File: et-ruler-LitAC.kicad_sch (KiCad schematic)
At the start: 27 parts, among them J1 Conn_01x03, J2 AudioJack2, J3 Pmod-Interface-GPIO6, J4 Pmod-Interface-GPIO6, SW1 SW_DPDT, U1 OP07

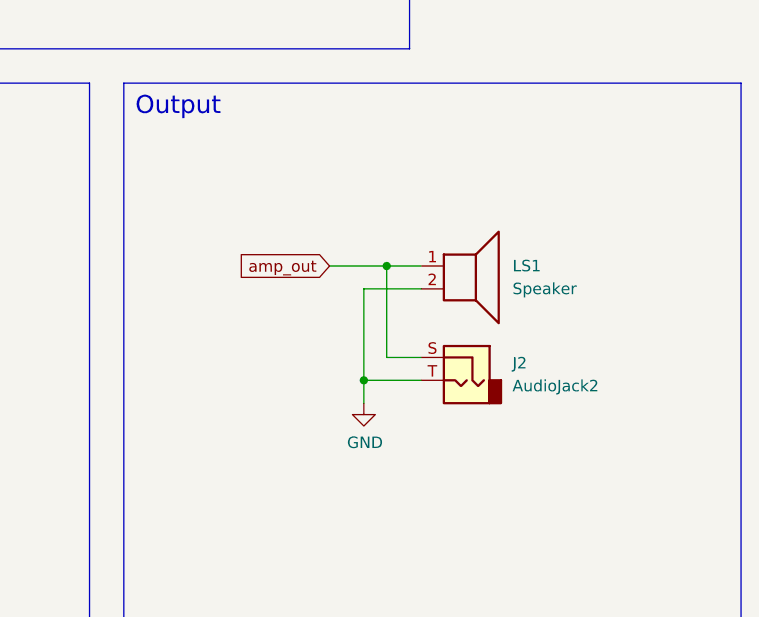
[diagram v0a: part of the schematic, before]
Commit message: Use correct audio jack
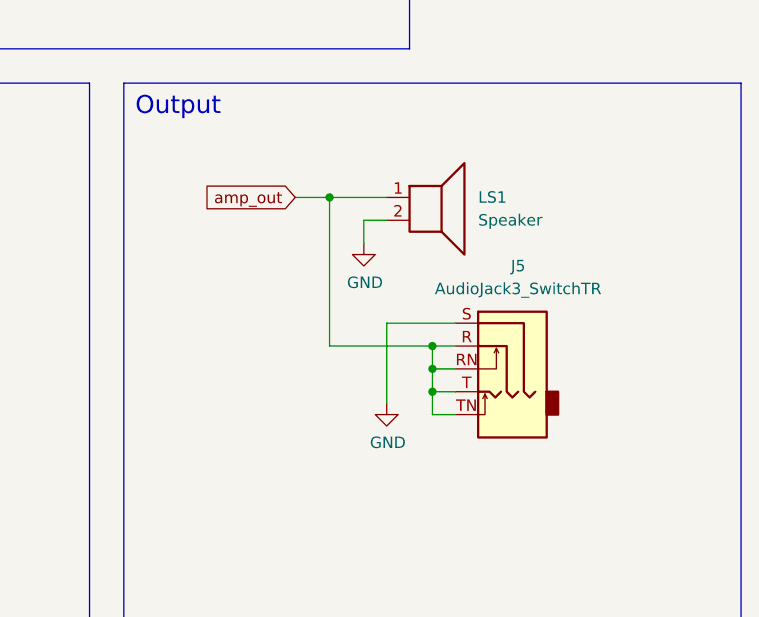
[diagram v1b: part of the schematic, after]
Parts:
- removed J2: AudioJack2, Connector_Audio:Jack_3.5mm_Ledino_KB3SPRS_Horizontal, symbol Connector:AudioJack2
- added J5: AudioJack3_SwitchTR, Connector_Audio:Jack_3.5mm_Ledino_KB3SPRS_Horizontal, symbol Connector_Audio:AudioJack3_SwitchTR
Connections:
- net GND: now also J5.S
- net amp_out: now also J5.R, J5.RN, J5.T, J5.TN
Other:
- moved on the sheet: LS1

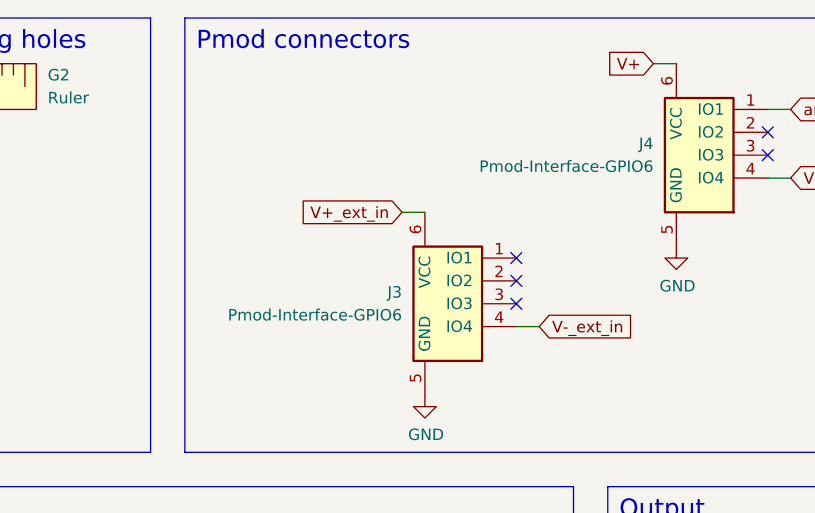
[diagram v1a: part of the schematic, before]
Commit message: Use pmod footprints from correct library
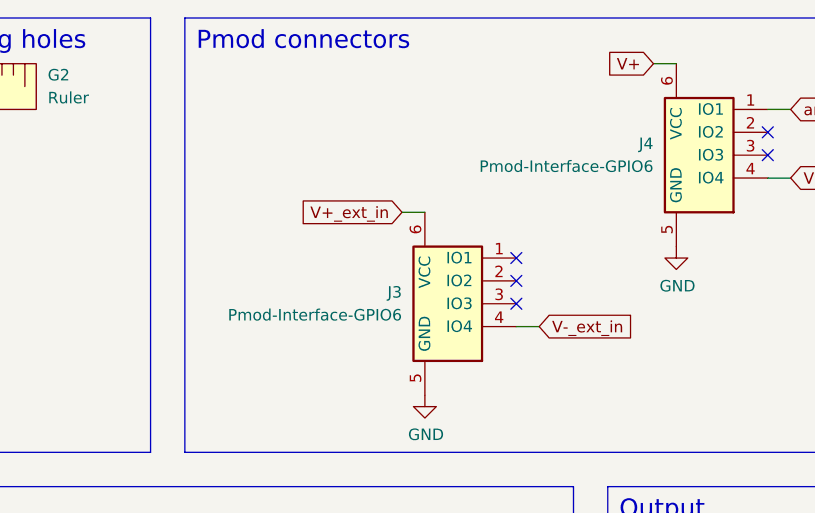
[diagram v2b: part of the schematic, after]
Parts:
- J3: footprint emt-pmod:Pmod_Interface_Male6 -> Pmod_Interface-emt:Pmod_Interface_Male6
- J4: footprint emt-pmod:Pmod_Interface_Female6 -> Pmod_Interface-emt:Pmod_Interface_Female6
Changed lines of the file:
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@@
   (symbol (lib_id "emt-pmos:Pmod-Interface-GPIO6") (at 180.34 49.53 0) (unit 1)
     (in_bom yes) (on_board yes) (dnp no) (fields_autoplaced)
-    (property "Reference" "J3" (at 175.26 48.2599 0)
+    (property "Reference" "J3" (at 175.26 48.26 0)
       (effects (font (size 1.27 1.27)) (justify right))
     )
-    (property "Value" "Pmod-Interface-GPIO6" (at 175.26 50.7999 0)
+    (property "Value" "Pmod-Interface-GPIO6" (at 175.26 50.8 0)
       (effects (font (size 1.27 1.27)) (justify right))
     )
-    (property "Footprint" "emt-pmod:Pmod_Interface_Male6" (at 182.88 53.34 0)
+    (property "Footprint" "Pmod_Interface-emt:Pmod_Interface_Male6" (at 182.88 53.34 0)
       (effects (font (size 1.27 1.27)) hide)
     )
@@
   (symbol (lib_id "emt-pmos:Pmod-Interface-GPIO6") (at 208.28 33.02 0) (unit 1)
     (in_bom yes) (on_board yes) (dnp no) (fields_autoplaced)
-    (property "Reference" "J4" (at 203.2 31.7499 0)
+    (property "Reference" "J4" (at 203.2 31.75 0)
       (effects (font (size 1.27 1.27)) (justify right))
     )
-    (property "Value" "Pmod-Interface-GPIO6" (at 203.2 34.2899 0)
+    (property "Value" "Pmod-Interface-GPIO6" (at 203.2 34.29 0)
       (effects (font (size 1.27 1.27)) (justify right))
     )
-    (property "Footprint" "emt-pmod:Pmod_Interface_Female6" (at 210.82 36.83 0)
+    (property "Footprint" "Pmod_Interface-emt:Pmod_Interface_Female6" (at 210.82 36.83 0)
       (effects (font (size 1.27 1.27)) hide)
     )

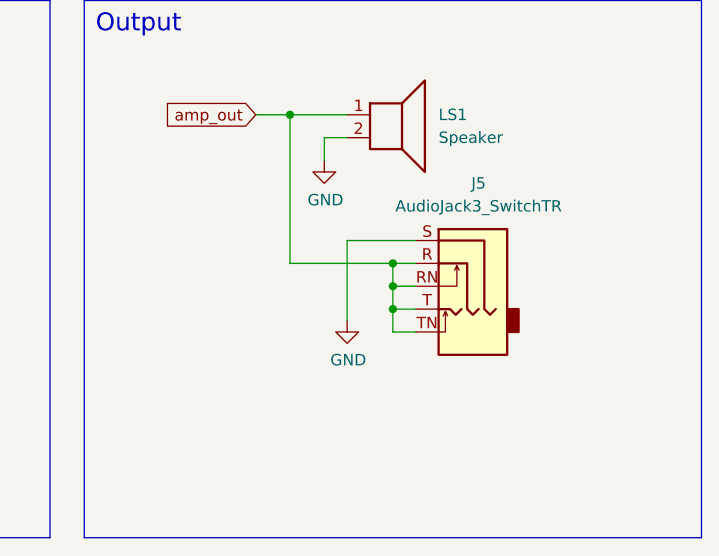
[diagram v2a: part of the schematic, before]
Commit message: Only connect tip/left channel of audio jack
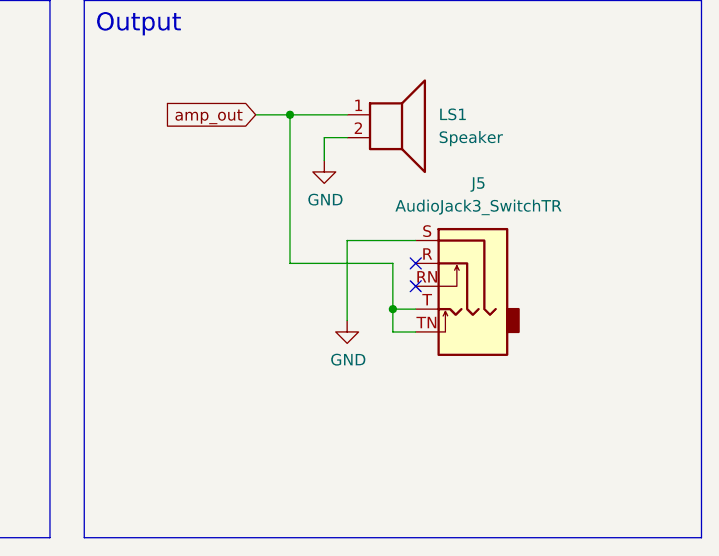
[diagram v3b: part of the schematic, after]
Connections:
- net amp_out: no longer J5.R, J5.RN
- no-connect marks 7 -> 9
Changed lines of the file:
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@@
   (junction (at 113.03 88.9) (diameter 0) (color 0 0 0 0)
   )
-  (junction (at 232.41 101.6) (diameter 0) (color 0 0 0 0)
-  )
   (junction (at 220.98 82.55) (diameter 0) (color 0 0 0 0)
   )
@@
   )
   (junction (at 149.86 105.41) (diameter 0) (color 0 0 0 0)
-  )
-  (junction (at 232.41 99.06) (diameter 0) (color 0 0 0 0)
   )
   (junction (at 232.41 104.14) (diameter 0) (color 0 0 0 0)
@@
   (no_connect (at 129.54 113.03))
   (no_connect (at 215.9 30.48))
+  (no_connect (at 234.95 99.06))
   (no_connect (at 187.96 44.45))
+  (no_connect (at 234.95 101.6))
   (no_connect (at 187.96 49.53))
   (wire (pts (xy 215.9 27.94) (xy 218.44 27.94))
     (stroke (width 0) (type default))
   )
-  (wire (pts (xy 232.41 101.6) (xy 232.41 99.06))
-    (stroke (width 0) (type default))
-  )
   (polyline (pts (xy 93.98 66.04) (xy 147.32 66.04))
     (stroke (width 0) (type default))
@@
     (stroke (width 0) (type default))
   )
-  (wire (pts (xy 234.95 101.6) (xy 232.41 101.6))
-    (stroke (width 0) (type default))
-  )
   (wire (pts (xy 149.86 105.41) (xy 152.4 105.41))
     (stroke (width 0) (type default))
@@
     (stroke (width 0) (type default))
   )
-  (wire (pts (xy 232.41 104.14) (xy 232.41 101.6))
+  (wire (pts (xy 232.41 99.06) (xy 232.41 104.14))
     (stroke (width 0) (type default))
   )
@@
     (stroke (width 0) (type default))
   )
-  (wire (pts (xy 232.41 99.06) (xy 234.95 99.06))
-    (stroke (width 0) (type default))
-  )
